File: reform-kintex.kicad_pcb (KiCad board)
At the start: 8 copper layers, 68 x 67.8 mm, 331 parts, among them J1 Conn_01x33, J2 JTAG_01x06, U1 MNT Reform 2.0 SoM Socket, U10 W25Q128JVS, U11 TPS62823DLC, U12 TPS62823DLC, U13 TPS62823DLC, U14 TPS62823DLC, U15 TPS62823DLC, U16 TPS62823DLC, U17 Si52112-B6, U2 XC7K160T-FFG676, U3 IS43TR16512B-125KBLI, U4 IS43TR16512B-125KBLI, U5 TPS51200DRC, U6 KSZ9031RNXCA, U7 TUSB1310ZAY, U8 TC358778XBG, U9 SiI9022A

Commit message: place lots of caps; place some power supplies
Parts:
- added C189: 4.7uF, Capacitor_SMD:C_0402_1005Metric, F.Cu at (159.2, 90.5)
- added C190: 4.7uF, Capacitor_SMD:C_0402_1005Metric, F.Cu at (162.1, 88.5)
- added J3: Conn_01x03_Male, Connector_PinHeader_2.00mm:PinHeader_1x03_P2.00mm_Horizontal, F.Cu at (186.0, 150.5)
- added Y1: ABM8G-25.000MHZ-18-D2Y-T, Crystal:Crystal_SMD_3225-4Pin_3.2x2.5mm, F.Cu at (146.2, 109.5)
- added Y2: ABM8G-20.000MHZ-18-D2Y-T, Crystal:Crystal_SMD_3225-4Pin_3.2x2.5mm, F.Cu at (163.0, 115.8)
- C114, C115, C121, C122, C123, C124, C125, C126, C127, C128, C129, C166, C167, C168, C169, C170, C171, C172, C173, C174, C175, C176, C177, C178, C179, C180, C181, C182, C183, C184, C185, C186, C187, C188, C82, C83, C85, C86, C87, C88, C90, C91, C92, R56, R57, R58, R60: moved to B.Cu
- C117: value 0.1uF -> 4.7uF
- moved R81 114.0 mm to (183.8, 155.0), turned to 90 degrees
- moved TP1 82.9 mm to (185.7, 115.6)
- moved TP11 82.9 mm to (188.7, 116.2)
- moved TP12 82.9 mm to (185.7, 118.7)
- moved TP4 82.9 mm to (175.2, 129.2)
- moved R35 82.1 mm to (95.0, 146.0)
- moved TP10 81.4 mm to (183.2, 118.5)
- moved TP3 81.4 mm to (183.2, 115.4)
- moved TP5 81.4 mm to (183.2, 121.5)
- moved C127 80.8 mm to (160.8, 145.0)
- moved TP7 79.9 mm to (181.5, 123.8)
- moved TP8 78.9 mm to (180.5, 120.8)
- moved C125 75.5 mm to (164.8, 145.0)
- moved C128 75.2 mm to (162.8, 145.0), turned to 180 degrees
- moved C124 75.1 mm to (167.0, 140.0), turned to 270 degrees
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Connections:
- C117 pad 1: +1V2 -> GND
- C117 pad 2: GND -> +5V
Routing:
- net Net-(R21-Pad1): track 0.71 -> 10.5 mm
- net Net-(C36-Pad1): track 0.57 -> 10.1 mm
- net Net-(R19-Pad1): track 0.71 -> 9.20 mm
- net Net-(C35-Pad1): track 0.57 -> 8.36 mm
- net Net-(J2-Pad3): track 0.71 -> 8.05 mm
- net Net-(R20-Pad1): track 0.71 -> 6.96 mm
- net TUSB_VSSOSC: track 0.57 -> 4.64 mm
- net DISP1_RGB21: track 15.9 -> 16.8 mm
- net RAM_DM1: track 55.7 -> 54.8 mm
- net GND: vias 186 -> 192
- added copper zone on F.Cu, net GND

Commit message: place all components
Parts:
- removed C88: 0.1uF, Capacitor_SMD:C_0402_1005Metric
- C1, C100, C101, C102, C103, C104, C105, C106, C107, C108, C109, C111, C112, C2, C24, C25, C27, C28, C3, C43, C44, C45, C68, C73, C84, C89, C93, C94, C95, C96, C97, C98, C99, FB1, FB2, FB3, R85, TP10, TP11, TP12, TP7, TP8, TP9: moved to B.Cu
- R23: moved to F.Cu
- moved C190 82.0 mm to (111.2, 152.8)
- moved TP6 76.4 mm to (116.8, 157.8)
- moved TP5 75.8 mm to (108.2, 132.8)
- moved R25 69.9 mm to (110.0, 161.2), turned to 270 degrees
- moved D1 69.0 mm to (112.2, 163.5)
- moved D2 67.1 mm to (112.3, 161.3)
- moved R24 66.4 mm to (110.0, 163.5), turned to 270 degrees
- moved TP3 65.7 mm to (118.0, 107.2)
- moved C80 61.0 mm to (114.8, 154.0)
- moved J3 56.1 mm to (132.2, 166.5), turned to 180 degrees
- moved R79 55.9 mm to (118.5, 163.2)
- moved C10 55.7 mm to (147.8, 106.8)
- moved R80 54.9 mm to (116.2, 163.2)
- moved TP4 53.8 mm to (127.5, 104.5)
- moved C1 53.6 mm to (132.5, 140.5)
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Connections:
- U2 pad A10: SD2_DATA2 -> SD2_CD
- U2 pad A12: SD2_CD -> SD2_DATA2
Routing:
- net DAC_RXFS: track 19.5 -> 51.9 mm
- net DAC_DIN: track 21.1 -> 53.5 mm
- net DAC_BCLK: track 21.1 -> 53.3 mm
- net DAC_TXFS: track 19.9 -> 52.1 mm
- net DAC_DOUT: track 18.6 -> 50.6 mm
- net DAC_MCLK: track 21.4 -> 53.4 mm
- net +5V: track 57.7 -> 78.7 mm, vias 0 -> 1
- net SD2_DATA1: track 29.1 -> 40.3 mm
- net SD2_DATA2: track 29.1 -> 36.3 mm
- net Net-(C16-Pad1): track 0.00 -> 6.97 mm
- net Net-(C13-Pad1): track 0.00 -> 6.97 mm
- net SD2_CLK: track 32.0 -> 37.9 mm
- net VTTREF: track 17.6 -> 21.9 mm
- net SD2_CD: track 29.0 -> 33.1 mm
- net Net-(L6-Pad1): track 0.00 -> 3.15 mm
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
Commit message: more routing
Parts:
- C118, R22: moved to B.Cu
- moved C40 29.2 mm to (147.4, 111.9)
- moved R23 23.3 mm to (96.7, 131.6)
- moved R22 8.28 mm to (127.0, 131.0)
- moved C39 1.63 mm to (150.6, 113.6)
- moved R98 1.11 mm to (118.6, 124.6), turned to 180 degrees
- moved R95 1.06 mm to (131.6, 110.2)
- moved C55 1.00 mm to (120.8, 129.7)
- moved C185 0.70 mm to (154.5, 116.8)
- moved C186 0.70 mm to (153.2, 116.8)
- moved C184 0.64 mm to (150.5, 123.9)
- moved C82 0.55 mm to (130.0, 103.3)
- moved R49 0.35 mm to (121.6, 109.2)
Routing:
- net +1V8: track 49.4 -> 241.5 mm, vias 53 -> 59
- net GND: track 166.7 -> 344.2 mm, vias 191 -> 203
- net Net-(R19-Pad1): track 9.20 -> 69.3 mm, vias 1 -> 2
- net +3V3: track 13.8 -> 73.4 mm, vias 15 -> 16
- net MODE2: track 0.71 -> 58.3 mm
- net Net-(R21-Pad1): track 10.5 -> 67.5 mm, vias 1 -> 2
- net Net-(J2-Pad3): track 8.05 -> 60.1 mm
- net +5V: track 78.7 -> 130.7 mm, vias 1 -> 2
- net Net-(R20-Pad1): track 6.96 -> 56.2 mm, vias 1 -> 2
- net +1V1: track 13.0 -> 60.0 mm, vias 23 -> 25
- net ETH0_LED_RX: track 26.2 -> 68.7 mm
- net MODE0: track 0.71 -> 40.9 mm, vias 1 -> 2
- net MODE1: track 0.71 -> 39.2 mm, vias 1 -> 2
- net UART2_TX: track 27.2 -> 59.8 mm, vias 1 -> 3
- net UART1_RX: track 29.3 -> 60.6 mm, vias 1 -> 3
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
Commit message: more routing
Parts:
- C110, C113, C119, C120, R23, R98: moved to B.Cu
- C73: moved to F.Cu
- moved R76 53.6 mm to (112.8, 163.0)
- moved R75 47.8 mm to (112.8, 158.2)
- moved R97 39.7 mm to (106.2, 165.2), turned to 0 degrees
- moved R23 31.3 mm to (128.0, 130.0)
- moved C73 20.7 mm to (122.3, 112.8), turned to 0 degrees
- moved R29 20.3 mm to (149.5, 107.2), turned to 270 degrees
- moved C55 17.9 mm to (132.8, 143.0), turned to 0 degrees
- moved C7 17.1 mm to (119.7, 117.6)
- moved C6 17.1 mm to (119.7, 116.6)
- moved R17 13.3 mm to (130.0, 133.0), turned to 270 degrees
- moved R18 12.2 mm to (129.0, 131.0), turned to 90 degrees
- moved TP7 11.3 mm to (135.0, 132.5)
- moved R98 7.95 mm to (126.5, 125.5)
- moved C114 5.05 mm to (115.7, 119.4), turned to 270 degrees
- moved R24 4.01 mm to (110.2, 159.5), turned to 90 degrees
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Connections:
- U2 pad D9: DISP1_RGB10 -> DISP1_RGB7
- U2 pad F10: DISP1_RGB7 -> DISP1_RGB11
- U2 pad F14: DISP1_RGB11 -> DISP1_RGB8
- U2 pad G10: DISP1_RGB21 -> DISP1_RGB17
- U2 pad G11: DISP1_RGB8 -> DISP1_RGB13
- U2 pad G14: DISP1_RGB14 -> DISP1_RGB10
- U2 pad G9: DISP1_RGB20 -> DISP1_RGB15
- U2 pad H11: DISP1_RGB12 -> DISP1_RGB14
- U2 pad H12: DISP1_RGB13 -> DISP1_RGB19
- U2 pad H13: DISP1_RGB18 -> DISP1_RGB16
- U2 pad H14: DISP1_RGB15 -> DISP1_RGB12
- U2 pad H8: DISP1_RGB22 -> DISP1_RGB21
- U2 pad H9: DISP1_RGB23 -> DISP1_RGB22
- U2 pad J10: DISP1_RGB16 -> DISP1_RGB20
- U2 pad J11: DISP1_RGB17 -> DISP1_RGB23
- U2 pad J13: DISP1_RGB19 -> DISP1_RGB18
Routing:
- net GND: track 344.2 -> 431.6 mm, vias 203 -> 209
- net +3V3: track 73.4 -> 143.5 mm, vias 16 -> 18
- net +1V8: track 241.5 -> 306.0 mm, vias 59 -> 61
- net BACKLIGHT_PWM: track 0.71 -> 62.8 mm, vias 1 -> 2
- net Net-(D1-Pad2): track 0.71 -> 57.0 mm, vias 1 -> 2
- net Net-(D2-Pad2): track 0.71 -> 54.3 mm, vias 1 -> 2
- net +1V5: track 198.4 -> 251.2 mm
- net CCLK: track 0.71 -> 31.4 mm, vias 1 -> 3
- net PCIE2_TX_P: track 0.00 -> 28.3 mm, vias 0 -> 2
- net PCIE2_TX_N: track 0.00 -> 28.3 mm, vias 0 -> 2
- net +1V2: track 16.8 -> 42.8 mm, vias 12 -> 17
- net UART3_TX: track 50.1 -> 27.0 mm, vias 3 -> 2
- net UART3_RX: track 49.4 -> 27.0 mm, vias 3 -> 2
- net PCIE1_CLK_N: track 0.00 -> 21.9 mm, vias 0 -> 1
- net PCIE1_CLK_P: track 0.00 -> 20.6 mm, vias 0 -> 1
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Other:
- board text removed: "dnp"

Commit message: more routing: 215 to go
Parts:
- added C191: 22pF, Capacitor_SMD:C_0402_1005Metric, F.Cu at (109.5, 112.2)
- added C88: 22pF, Capacitor_SMD:C_0402_1005Metric, F.Cu at (109.5, 110.2)
- added Y3: ABM8G-25.000MHZ-18-D2Y-T, Crystal:Crystal_SMD_3225-4Pin_3.2x2.5mm, F.Cu at (112.2, 111.4)
- C172, C173, C175, C187, C188: moved to F.Cu
- R30, R31, R61, R62, R63, R64, R66, R67, R68, R69, R70, R72, R73: moved to B.Cu
- moved R58 23.6 mm to (157.5, 110.6), turned to 90 degrees
- moved R69 15.8 mm to (157.9, 117.1), turned to 270 degrees
- moved R73 12.4 mm to (159.9, 122.4), turned to 0 degrees
- moved R30 11.4 mm to (152.5, 103.1)
- moved R31 11.4 mm to (150.5, 103.1)
- moved R70 9.88 mm to (155.8, 122.9)
- moved R57 5.14 mm to (160.4, 126.1), turned to 90 degrees
- moved R27 4.25 mm to (156.8, 103.0), turned to 270 degrees
- moved TP2 4.24 mm to (159.2, 112.5)
- moved R61 4.20 mm to (153.8, 132.8)
- moved C72 3.78 mm to (126.0, 111.8)
- moved C73 3.73 mm to (126.0, 112.9)
- moved C124 3.40 mm to (163.6, 140.0)
- moved C75 3.30 mm to (116.2, 109.3), turned to 180 degrees
- moved C119 3.04 mm to (108.3, 118.7)
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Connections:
- net Net-(C70-Pad2) renamed /RAM/PCIE2_GTX_CLK_HOST_P
- net Net-(C71-Pad2) renamed /RAM/PCIE2_GTX_CLK_HOST_N
- net Net-(C72-Pad2) renamed /RAM/PCIE2_GTX_CLK_P
- net Net-(C73-Pad2) renamed /RAM/PCIE2_GTX_CLK_N
- net Net-(C8-Pad2) renamed /RAM/USB2_GTX_N
- net Net-(C9-Pad2) renamed /RAM/USB2_GTX_P
- U2 pad K18: DAC_MCLK -> DAC_RXFS
- U2 pad L17: DAC_TXFS -> DAC_BCLK
- U2 pad L18: DAC_BCLK -> DAC_MCLK
- U2 pad M16: DAC_DOUT -> DAC_TXFS
- U2 pad M17: DAC_RXFS -> DAC_DOUT
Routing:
- net GND: track 431.6 -> 684.6 mm, vias 209 -> 280
- net +1V8: track 306.0 -> 399.1 mm, vias 61 -> 66
- net +1V2: track 42.8 -> 105.7 mm, vias 17 -> 20
- net +3V3: track 143.5 -> 203.8 mm, vias 18 -> 22
- net VTTREF: track 34.5 -> 83.0 mm, vias 8 -> 10
- net USB2_RX_P: track 8.63 -> 55.9 mm, vias 2 -> 3
- net USB2_RX_N: track 7.05 -> 54.2 mm, vias 2 -> 3
- net /RAM/USB2_GTX_N: track 0.71 -> 44.7 mm, vias 1 -> 4
- net /RAM/USB2_GTX_P: track 0.71 -> 44.0 mm, vias 1 -> 4
- net ETH0_LED_LINK1: track 26.8 -> 63.9 mm
- net +1V1: track 60.0 -> 96.5 mm, vias 25 -> 26
- net PCIE2_CLK_N: track 16.6 -> 40.3 mm, vias 1 -> 3
- net +1V5: track 251.2 -> 273.7 mm, vias 48 -> 51
- net PCIE2_CLK_P: track 16.1 -> 37.8 mm, vias 1 -> 3
- net FCS_B: track 0.71 -> 21.5 mm, vias 1 -> 2
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
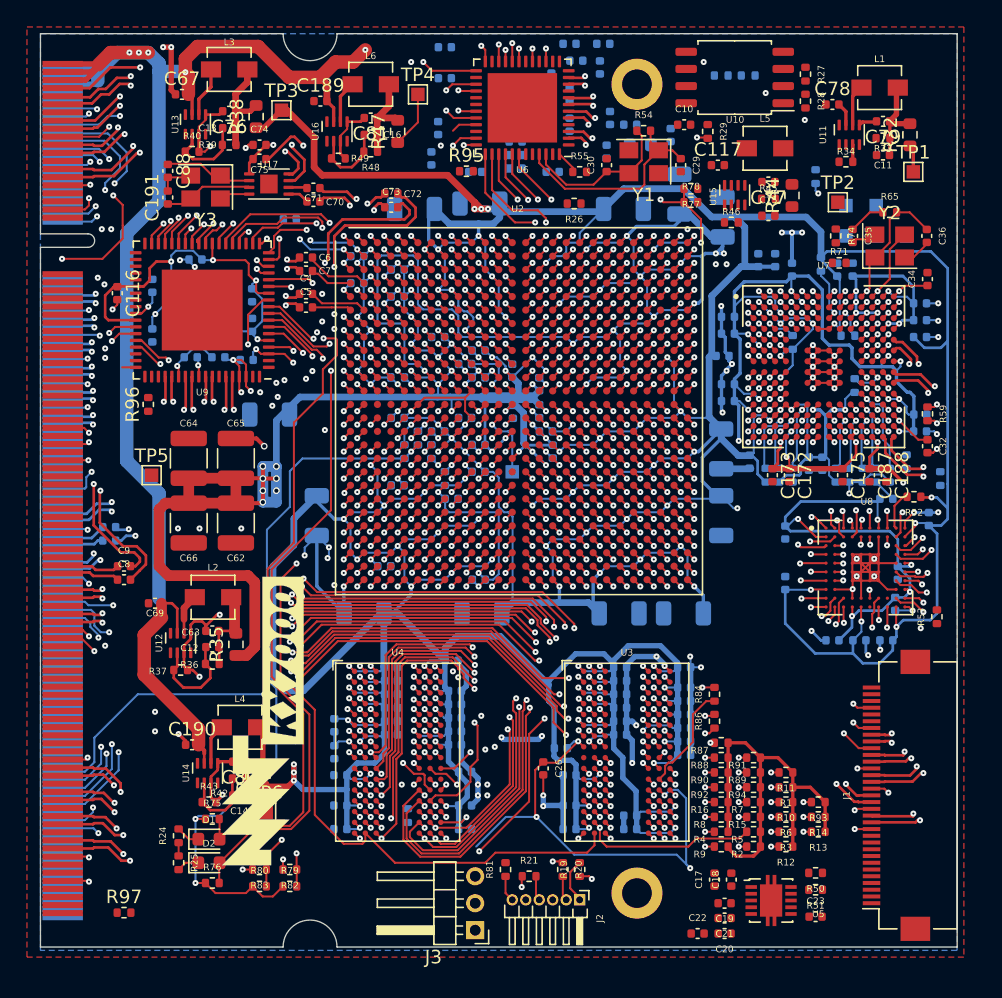
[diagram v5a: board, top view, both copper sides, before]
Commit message: add power sequencer, main clock, some missing resets, more routing (198)
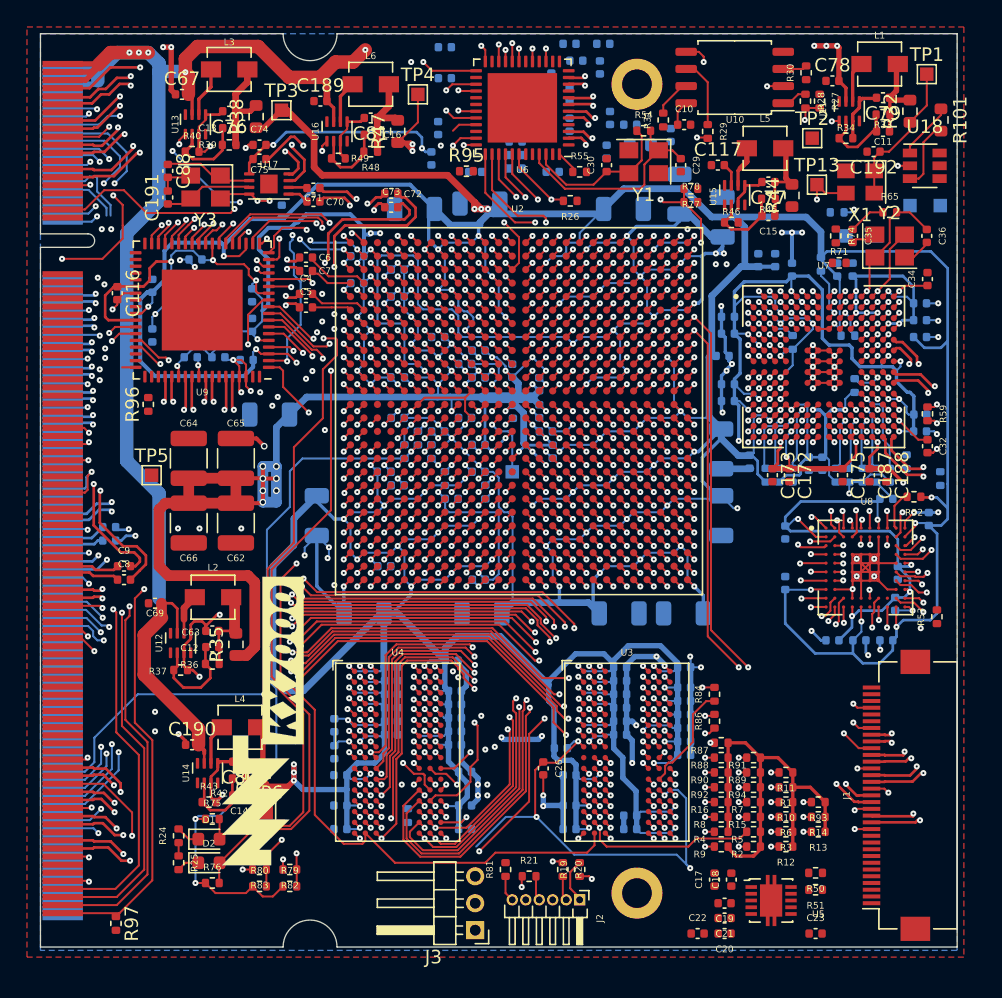
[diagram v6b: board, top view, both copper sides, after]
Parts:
- added C192: 0.1uF, Capacitor_SMD:C_0402_1005Metric, F.Cu at (161.8, 108.8)
- added R100: 80.6, Resistor_SMD:R_0402_1005Metric, B.Cu at (133.0, 134.0)
- added R101: 0, Resistor_SMD:R_0603_1608Metric, F.Cu at (166.8, 106.4)
- added R99: 80.6, Resistor_SMD:R_0402_1005Metric, B.Cu at (125.5, 132.5)
- added TP13: TestPoint, TestPoint:TestPoint_Pad_1.0x1.0mm, F.Cu at (157.6, 111.2)
- added U18: LM3880, Package_TO_SOT_SMD:SOT-23-6, F.Cu at (165.6, 109.8)
- added X1: ASFLMB-100.000MHZ-XY-T, Oscillator:Oscillator_SMD_Abracon_ASE-4Pin_3.2x2.5mm, F.Cu at (160.8, 111.0)
- R30, R31: moved to F.Cu
- moved TP1 7.32 mm to (165.8, 103.0)
- moved R31 5.42 mm to (146.2, 106.4), turned to 90 degrees
- moved TP2 5.12 mm to (157.2, 107.8)
- moved TP10 4.75 mm to (166.8, 112.8)
- moved TP8 4.75 mm to (164.5, 112.8)
- moved R30 4.30 mm to (156.8, 102.9), turned to 90 degrees
- moved R58 3.10 mm to (159.1, 113.2), turned to 180 degrees
- moved R27 2.26 mm to (157.8, 105.0)
- moved C11 1.75 mm to (162.5, 107.2)
- moved C78 1.75 mm to (158.8, 103.5)
- moved C79 1.75 mm to (162.5, 104.8)
- moved L1 1.75 mm to (162.2, 102.2)
- moved R32 1.75 mm to (164.5, 105.8)
- moved R33 1.75 mm to (162.5, 106.0)
- moved R34 1.75 mm to (159.8, 107.8)
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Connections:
- U11 pad 1: Net-(U11-Pad1) -> EN_VIO
- U12 pad 1: Net-(U12-Pad1) -> +5V
- U13 pad 1: Net-(U13-Pad1) -> EN_VIO
- U14 pad 1: Net-(U14-Pad1) -> EN_VDDR
- U15 pad 1: Net-(U15-Pad1) -> EN_VAUX
- U16 pad 1: Net-(U16-Pad1) -> EN_VIO
- U2 pad A13: Net-(U2-PadA13) -> DISP1_SDA
- U2 pad A17: Net-(U2-PadA17) -> PCIE1_RESETn
- U2 pad A18: Net-(U2-PadA18) -> PCIE2_RESETn
- U2 pad AB26: Net-(U2-PadAB26) -> DSI_RST_N
- U2 pad C13: Net-(U2-PadC13) -> HDMI_RST_N
- U2 pad F22: Net-(U2-PadF22) -> CLK_100MHZ
- U2 pad G12: Net-(U2-PadG12) -> DISP1_SCL
- U2 pad G26: Net-(U2-PadG26) -> I2C1_SCL
- U2 pad H26: Net-(U2-PadH26) -> I2C1_SDA
- U5 pad 7: Net-(U5-Pad7) -> EN_VDDR
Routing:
- net EN_VIO: track 0.00 -> 56.5 mm, vias 0 -> 3
- net +1V8: track 399.1 -> 443.9 mm, vias 66 -> 67
- net PCIE2_RESETn: track 3.01 -> 43.9 mm, vias 1 -> 4
- net PCIE1_RESETn: track 2.61 -> 40.8 mm, vias 1 -> 2
- net HDMI_RST_N: track 2.36 -> 39.1 mm, vias 1 -> 3
- net +1V2: track 105.7 -> 136.1 mm, vias 20 -> 24
- net HDMI_HPD: track 1.01 -> 31.1 mm, vias 0 -> 1
- net DISP1_SDA: track 0.00 -> 29.2 mm, vias 0 -> 3
- net I2C1_SCL: track 1.29 -> 29.6 mm, vias 1 -> 3
- net GND: track 684.6 -> 712.9 mm, vias 280 -> 287
- net HDMI_CEC: track 3.06 -> 31.0 mm, vias 1 -> 2
- net I2C1_SDA: track 0.64 -> 27.7 mm, vias 1 -> 3
- net HDMI_SCL: track 1.99 -> 28.6 mm, vias 1 -> 2
- net HDMI_SDA: track 2.15 -> 28.3 mm, vias 1 -> 2
- net DISP1_SCL: track 0.00 -> 25.1 mm, vias 0 -> 2
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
